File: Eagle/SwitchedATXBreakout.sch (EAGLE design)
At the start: 37 parts, among them K1 ALF1P05, K2 ALF1P05, K3 ALF1P05, K4 ALF1P05, K5 ALF1P05, X1 22-23-2091, X2 5566-24

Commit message: More work on board
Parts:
- added U$1, U$2, U$3, U$4: 15-24-4449, con-molex-additional:15-24-4449
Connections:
- removed net PSU_GND: X2-15.S, X2-17.S, X2-18.S, X2-19.S, X2-24.S, X2-3.S, X2-5.S, X2-7.S
- net GND: now also U$12.P$1, U$13.P$1, U$22.P$1, U$23.P$1, U$32.P$1, U$33.P$1, U$42.P$1, U$43.P$1, X2-15.S, X2-17.S, X2-18.S, X2-19.S, X2-24.S, X2-3.S, X2-5.S, X2-7.S
- net PSU_12V: now also U$11.P$1, U$21.P$1, U$31.P$1, U$41.P$1
- net PSU_5V: now also U$14.P$1, U$24.P$1, U$34.P$1, U$44.P$1
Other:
- moved on the sheet: X1-1, X1-2, X1-3, X1-4, X1-5, X1-6, X1-7, X1-8, X1-9

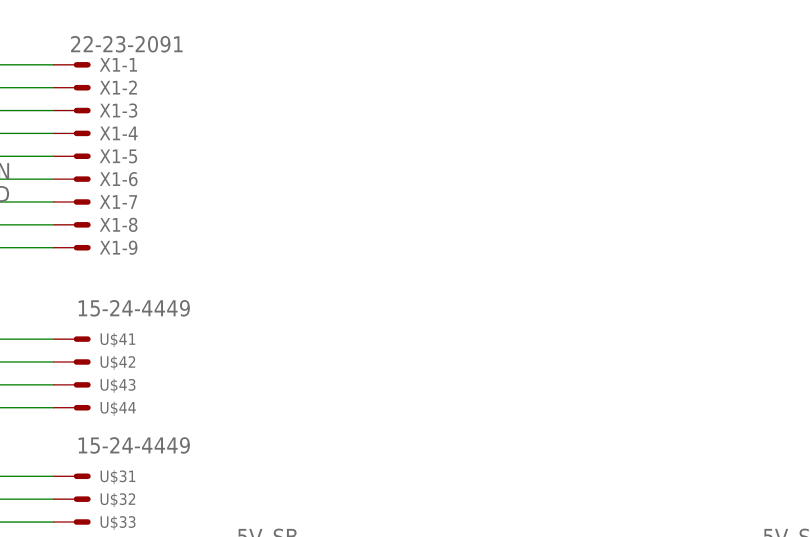
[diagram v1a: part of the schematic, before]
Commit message: Finish schematic
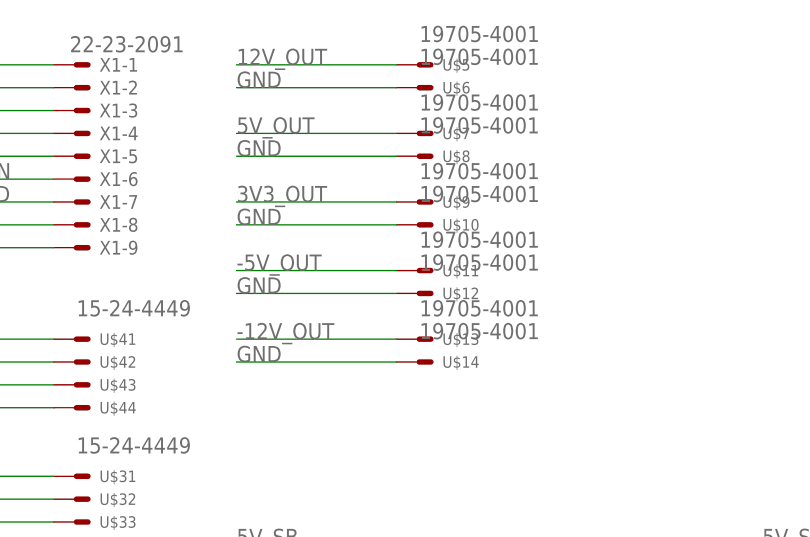
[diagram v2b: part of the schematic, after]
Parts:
- added U$10, U$11, U$12, U$13, U$14, U$5, U$6, U$7, U$8, U$9: 19705-4001, con-molex-additional:19705-4001
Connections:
- net -12V_OUT: now also U$13.P$1
- net -5V_OUT: now also U$11.P$1
- net 12V_OUT: now also U$5.P$1
- net 3V3_OUT: now also U$9.P$1
- net 5V_OUT: now also U$7.P$1
- net GND: now also U$10.P$1, U$12.P$1, U$14.P$1, U$6.P$1, U$8.P$1
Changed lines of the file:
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@@
 <part name="U$3" library="con-molex-additional" deviceset="15-24-4449" device=""/>
 <part name="U$4" library="con-molex-additional" deviceset="15-24-4449" device=""/>
+<part name="U$5" library="con-molex-additional" deviceset="19705-4001" device=""/>
+<part name="U$6" library="con-molex-additional" deviceset="19705-4001" device=""/>
+<part name="U$7" library="con-molex-additional" deviceset="19705-4001" device=""/>
+<part name="U$8" library="con-molex-additional" deviceset="19705-4001" device=""/>
+<part name="U$9" library="con-molex-additional" deviceset="19705-4001" device=""/>
+<part name="U$10" library="con-molex-additional" deviceset="19705-4001" device=""/>
+<part name="U$11" library="con-molex-additional" deviceset="19705-4001" device=""/>
+<part name="U$12" library="con-molex-additional" deviceset="19705-4001" device=""/>
+<part name="U$13" library="con-molex-additional" deviceset="19705-4001" device=""/>
+<part name="U$14" library="con-molex-additional" deviceset="19705-4001" device=""/>
 </parts>
 <sheets>
@@
 <instance part="U$4" gate="3" x="22.86" y="116.84"/>
 <instance part="U$4" gate="4" x="22.86" y="114.3"/>
+<instance part="U$5" gate="G$1" x="60.96" y="152.4"/>
+<instance part="U$6" gate="G$1" x="60.96" y="149.86"/>
+<instance part="U$7" gate="G$1" x="60.96" y="144.78"/>
+<instance part="U$8" gate="G$1" x="60.96" y="142.24"/>
+<instance part="U$9" gate="G$1" x="60.96" y="137.16"/>
+<instance part="U$10" gate="G$1" x="60.96" y="134.62"/>
+<instance part="U$11" gate="G$1" x="60.96" y="129.54"/>
+<instance part="U$12" gate="G$1" x="60.96" y="127"/>
+<instance part="U$13" gate="G$1" x="60.96" y="121.92"/>
+<instance part="U$14" gate="G$1" x="60.96" y="119.38"/>
 </instances>
 <busses>
@@
 <label x="2.54" y="25.4" size="1.778" layer="95"/>
 </segment>
+<segment>
+<pinref part="U$6" gate="G$1" pin="P$1"/>
+<wire x1="58.42" y1="149.86" x2="40.64" y2="149.86" width="0.1524" layer="91"/>
+<label x="40.64" y="149.86" size="1.778" layer="95"/>
+</segment>
+<segment>
+<pinref part="U$8" gate="G$1" pin="P$1"/>
+<wire x1="58.42" y1="142.24" x2="40.64" y2="142.24" width="0.1524" layer="91"/>
+<label x="40.64" y="142.24" size="1.778" layer="95"/>
+</segment>
+<segment>
+<pinref part="U$10" gate="G$1" pin="P$1"/>
+<wire x1="58.42" y1="134.62" x2="40.64" y2="134.62" width="0.1524" layer="91"/>
+<label x="40.64" y="134.62" size="1.778" layer="95"/>
+</segment>
+<segment>
+<pinref part="U$12" gate="G$1" pin="P$1"/>
+<wire x1="58.42" y1="127" x2="40.64" y2="127" width="0.1524" layer="91"/>
+<label x="40.64" y="127" size="1.778" layer="95"/>
+</segment>
+<segment>
+<pinref part="U$14" gate="G$1" pin="P$1"/>
+<wire x1="58.42" y1="119.38" x2="40.64" y2="119.38" width="0.1524" layer="91"/>
+<label x="40.64" y="119.38" size="1.778" layer="95"/>
+</segment>
 </net>
 <net name="N$3" class="0">
@@
 <label x="83.82" y="27.94" size="1.778" layer="95"/>
 </segment>
+<segment>
+<pinref part="U$5" gate="G$1" pin="P$1"/>
+<wire x1="58.42" y1="152.4" x2="40.64" y2="152.4" width="0.1524" layer="91"/>
+<label x="40.64" y="152.4" size="1.778" layer="95"/>
+</segment>
 </net>
 <net name="PSU_-12V" class="0">
@@
 <label x="83.82" y="83.82" size="1.778" layer="95"/>
 </segment>
+<segment>
+<pinref part="U$13" gate="G$1" pin="P$1"/>
+<wire x1="58.42" y1="121.92" x2="40.64" y2="121.92" width="0.1524" layer="91"/>
+<label x="40.64" y="121.92" size="1.778" layer="95"/>
+</segment>
 </net>
 <net name="-5V_OUT" class="0">
@@
 <label x="142.24" y="83.82" size="1.778" layer="95"/>
 </segment>
+<segment>
+<pinref part="U$11" gate="G$1" pin="P$1"/>
+<wire x1="58.42" y1="129.54" x2="40.64" y2="129.54" width="0.1524" layer="91"/>
+<label x="40.64" y="129.54" size="1.778" layer="95"/>
+</segment>
 </net>
 <net name="PSU_-5V" class="0">
@@
 <label x="142.24" y="27.94" size="1.778" layer="95"/>
 </segment>
+<segment>
+<pinref part="U$7" gate="G$1" pin="P$1"/>
+<wire x1="58.42" y1="144.78" x2="40.64" y2="144.78" width="0.1524" layer="91"/>
+<label x="40.64" y="144.78" size="1.778" layer="95"/>
+</segment>
 </net>
 <net name="PSU_3V3" class="0">
@@
 <label x="200.66" y="27.94" size="1.778" layer="95"/>
 </segment>
-</net>
+<segment>
+<pinref part="U$9" gate="G$1" pin="P$1"/>
+<wire x1="58.42" y1="137.16" x2="40.64" y2="137.16" width="0.1524" layer="91"/>
+<label x="40.64" y="137.16" size="1.778" layer="95"/>
+</segment>
+</net>

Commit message: Start board layout
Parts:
- removed U$3, U$4: 15-24-4449, con-molex-additional:15-24-4449
- LED1, LED2, LED3, LED4, LED5: device led:LED5MM -> led:LED3MM
- R1, R2, R3, R4, R5: value (none) -> 3K3; device resistor:R-EU_0204/5 -> resistor:R-EU_0204/7
- R10, R6, R7, R8, R9: value (none) -> 33K; device resistor:R-EU_0204/5 -> resistor:R-EU_0204/7
- R11, R12, R13, R14, R15: value (none) -> 120; device resistor:R-EU_0204/5 -> resistor:R-EU_0204/7
- T1, T2, T3, T4, T5: value (none) -> 2N3905; device transistor:-PNP-TO92 -> transistor:BC636-PNP-TO92-BCE
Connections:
- net GND: no longer U$32.P$1, U$33.P$1, U$42.P$1, U$43.P$1
- net N$11: now also T5.C; no longer T4.C
- net N$14: now also T3.C; no longer T5.C
- net N$2: now also T4.B; no longer T3.B
- net N$5: now also T5.B; no longer T4.B
- net N$7: now also T3.B; no longer T5.B
- net N$8: now also T4.C; no longer T3.C
- net PSU_12V: no longer U$31.P$1, U$41.P$1, X2-10.S, X2-11.S
- net PSU_5V: no longer U$34.P$1, U$44.P$1, X2-21.S, X2-22.S, X2-23.S, X2-4.S, X2-6.S
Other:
- moved on the sheet: T3, T4, T5

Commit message: Finish board layout
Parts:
- removed U$1, U$2: 15-24-4449, con-molex-additional:15-24-4449
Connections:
- net GND: no longer U$12.P$1, U$13.P$1, U$22.P$1, U$23.P$1
- net PSU_12V: now also X2-10.S, X2-11.S; no longer U$11.P$1, U$21.P$1
- net PSU_3V3: no longer X2-12.S
- net PSU_5V: now also X2-4.S, X2-6.S; no longer U$14.P$1, U$24.P$1
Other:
- moved on the sheet: U$10, U$11, U$12, U$13, U$14, U$5, U$6, U$7, U$8, U$9, X1-1, X1-2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

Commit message: Updated board layout
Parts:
- T1, T2, T3, T4, T5: value 2N3905 -> 2N3906; device transistor:BC636-PNP-TO92-BCE -> transistor-neu-to92:-PNP-TO92-EBC
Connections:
- net -12V_OUT: now also K41.S; no longer K31.S
- net -5V_OUT: now also K51.S; no longer K41.S
- net 3V3_OUT: now also K31.S; no longer K51.S
- net N$11: now also K5_.1; no longer K4_.1
- net N$12: now also LED3.A; no longer LED5.A
- net N$13: now also LED5.A; no longer LED4.A
- net N$14: now also K3_.1; no longer K5_.1
- net N$15: now also LED4.A; no longer LED3.A
- net N$8: now also K4_.1; no longer K3_.1
- net PSU_-12V: now also K41.P; no longer K31.P
- net PSU_-5V: now also K51.P; no longer K41.P
- net PSU_3V3: now also K31.P; no longer K51.P
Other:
- moved on the sheet: K3, K4, K5, LED3, LED4, LED5
